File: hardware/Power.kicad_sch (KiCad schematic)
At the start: 26 parts, among them Q1 Q_NMOS, Q2 Q_NMOS, Q3 Q_NMOS, Q4 Q_NMOS, U5 BQ25798RQMR

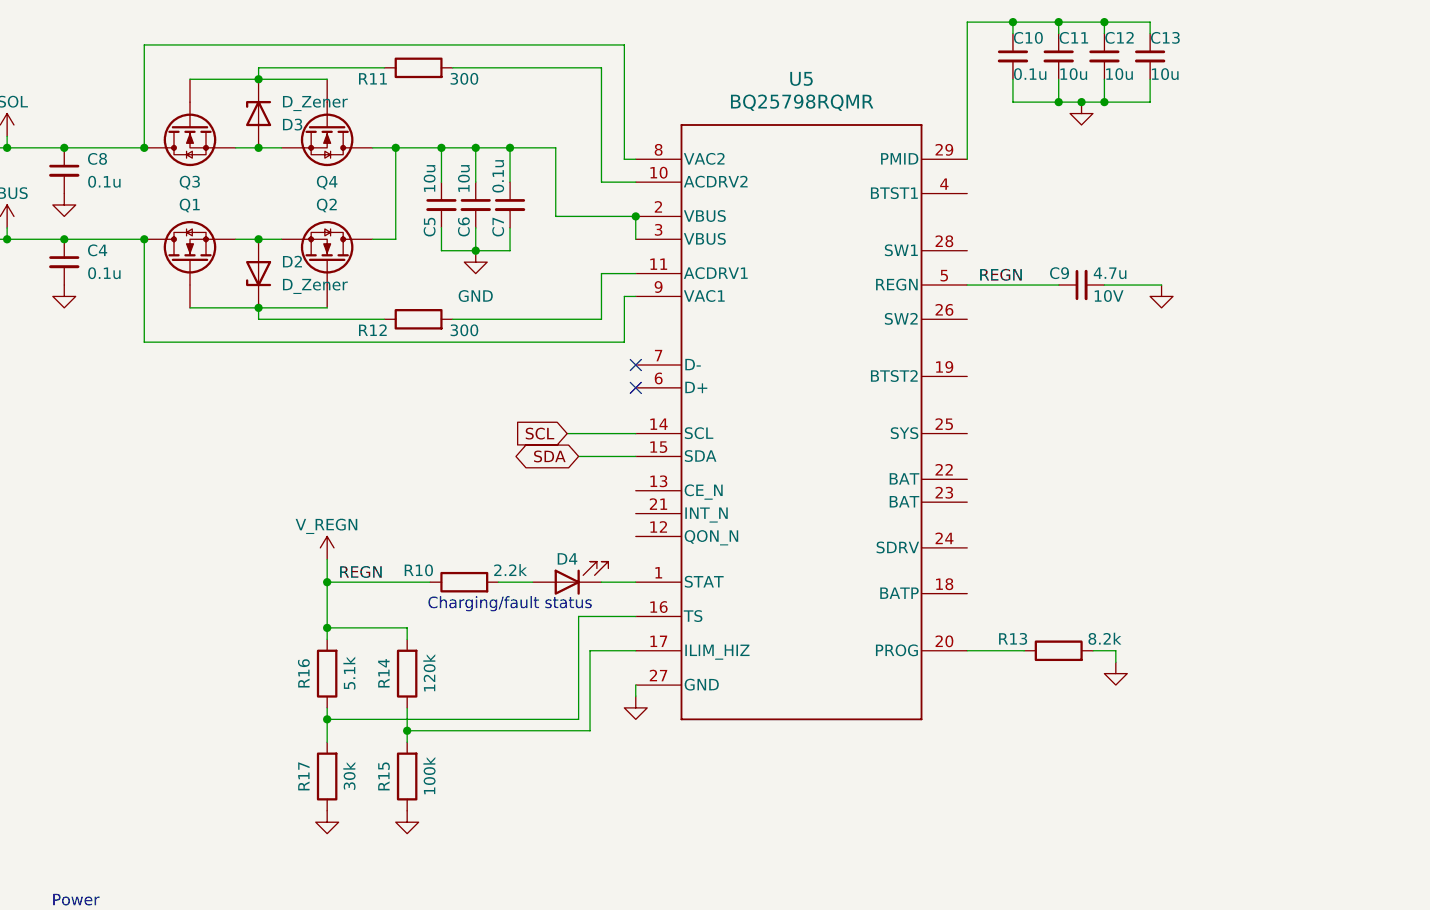
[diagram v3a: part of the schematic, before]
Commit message: Added BQ25798 integrated buck-boost inductor
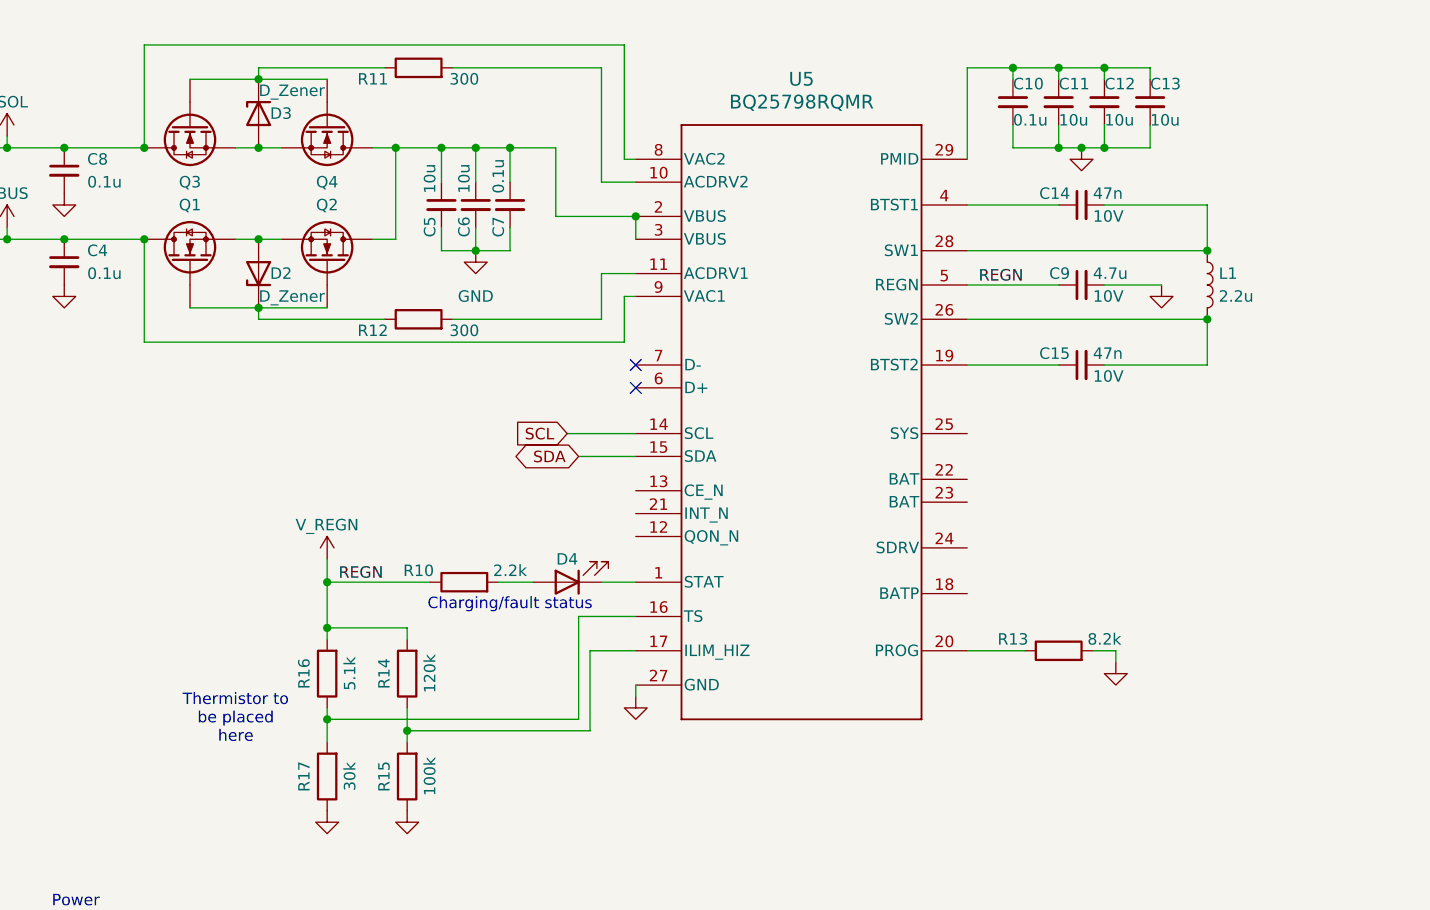
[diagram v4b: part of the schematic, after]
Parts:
- added C14, C15: 47n, Capacitor_SMD:C_0603_1608Metric, symbol Device:C_Small
- added L1: 2.2u, GoG_Library:MDA5030-2R2M, symbol Device:L
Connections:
- net at U5.19 (BTST2): now also C15.1
- net at U5.26 (SW2): now also C15.2, L1.2
- net at U5.28 (SW1): now also C14.2, L1.1
- net at U5.4 (BTST1): now also C14.1
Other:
- note added: "Thermistor to be placed here"
- moved on the sheet: C10, C11, C12, C13

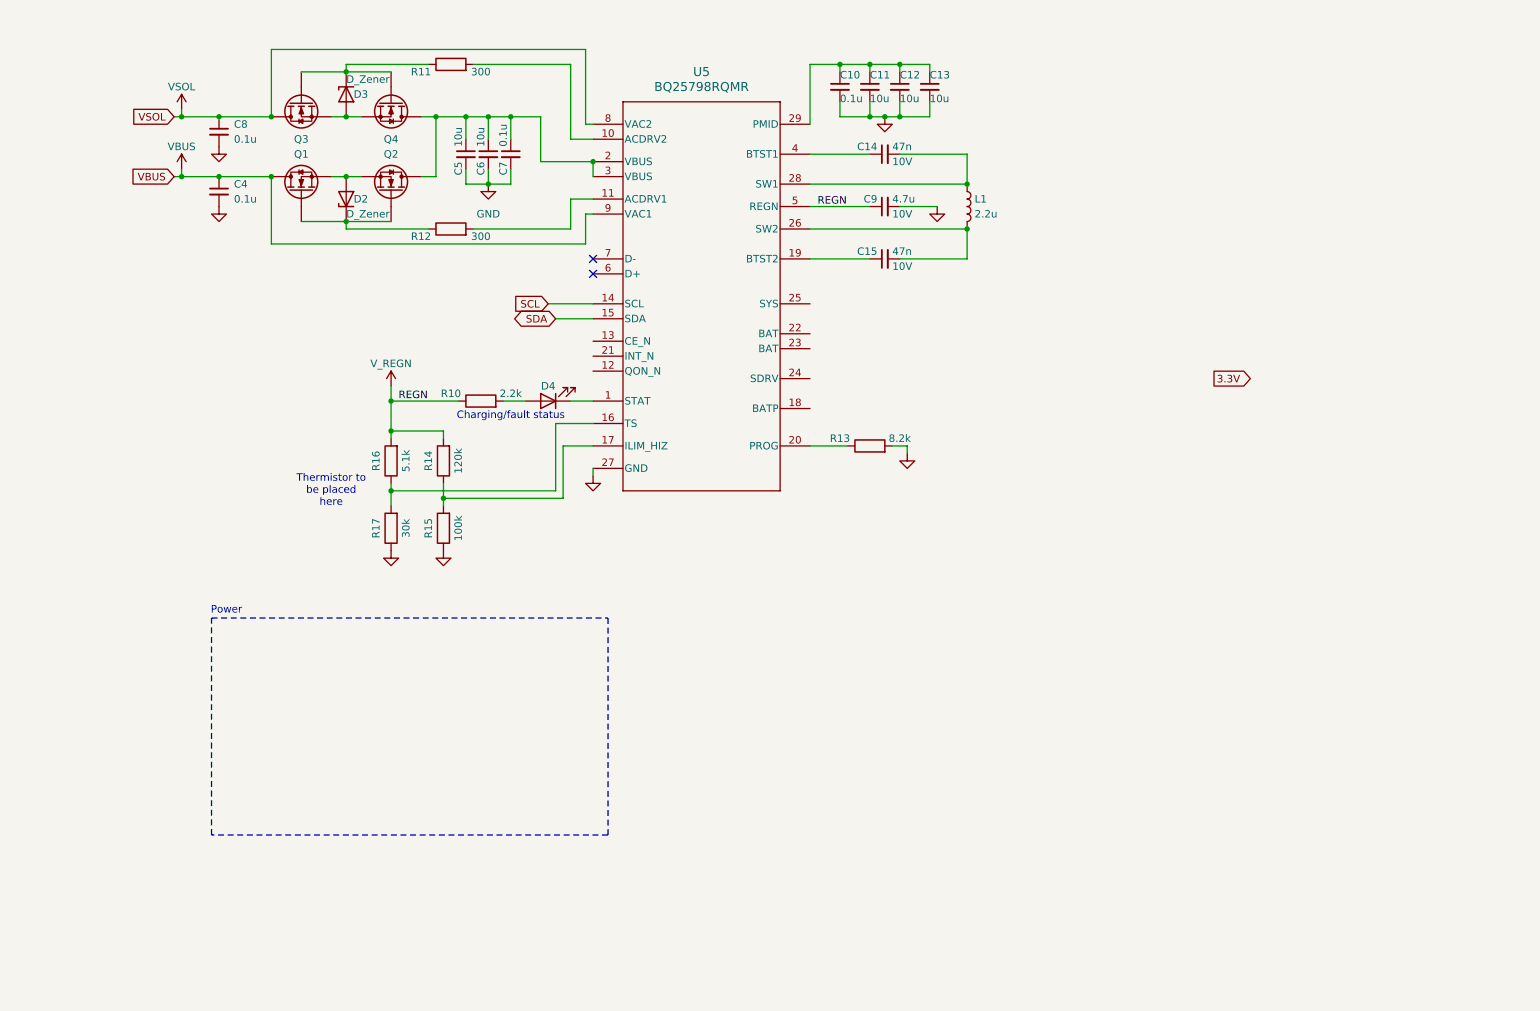
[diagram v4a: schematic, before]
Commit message: Add SYS output capacitors & cap. package sizes
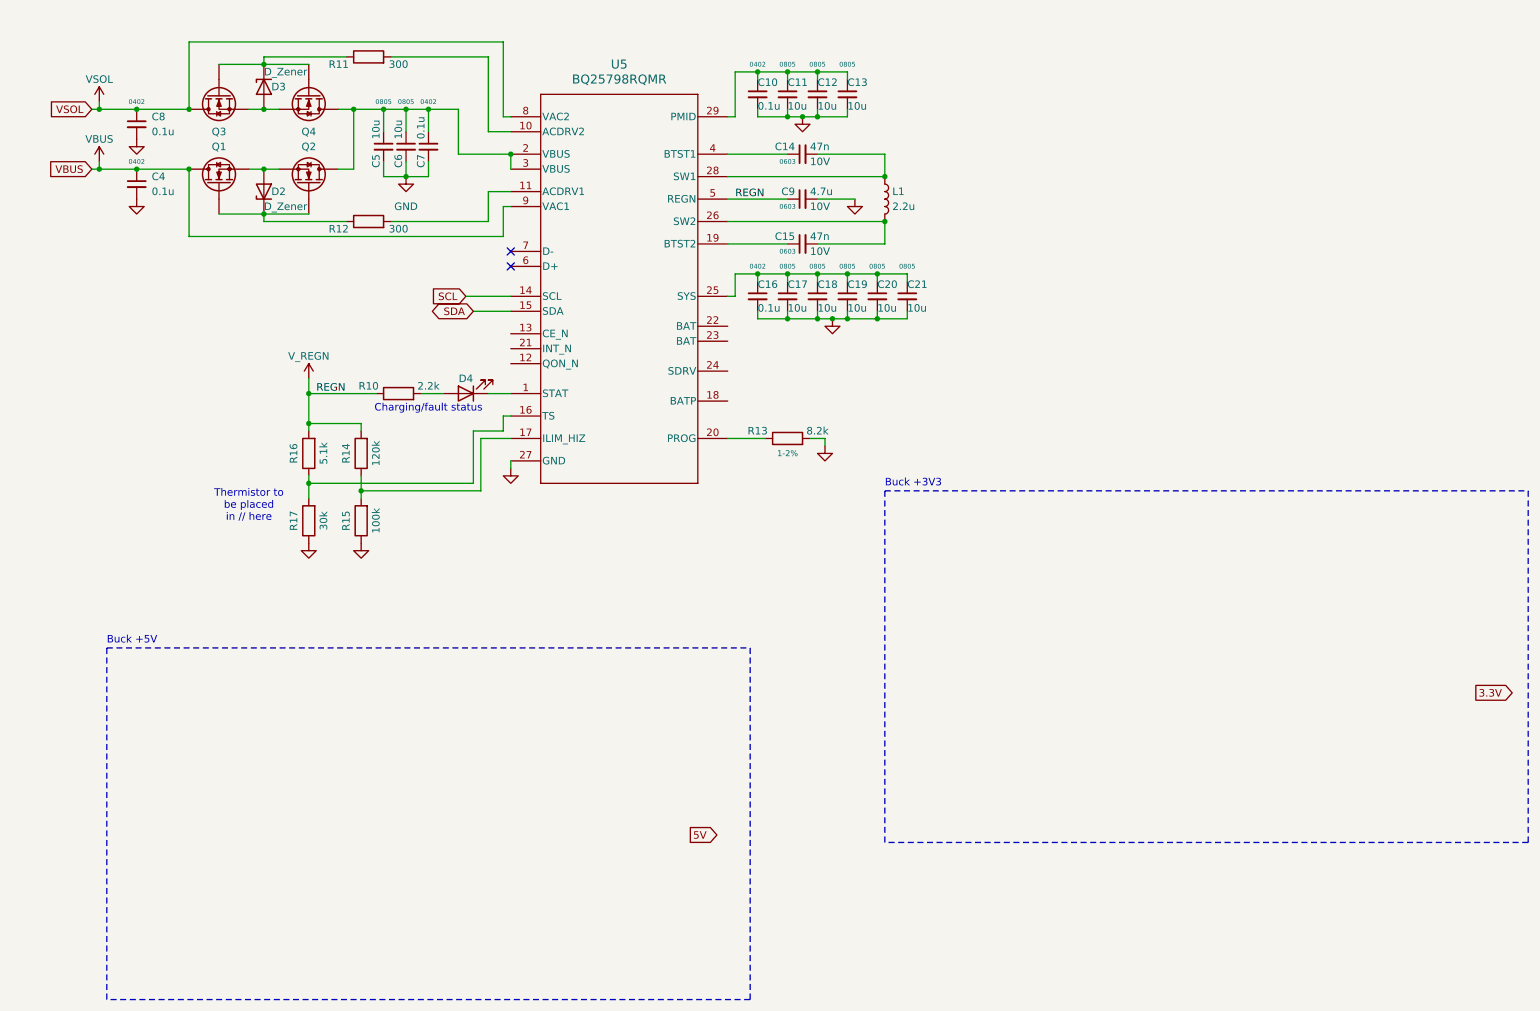
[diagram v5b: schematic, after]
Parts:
- added C16: 0.1u, Capacitor_SMD:C_0402_1005Metric, symbol Device:C_Small
- added C17, C18, C19, C20, C21: 10u, Capacitor_SMD:C_0805_2012Metric, symbol Device:C_Small
- C10, C4, C7, C8: Package (none) -> 0402
- C11, C12, C13, C5, C6: footprint Capacitor_SMD:C_0603_1608Metric -> Capacitor_SMD:C_0805_2012Metric; Package (none) -> 0805
- C14, C15, C9: Package (none) -> 0603
- R13: Tolerence (none) -> 1-2%
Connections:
- net GND: now also C16.2, C17.2, C18.2, C19.2, C20.2, C21.2
- net at U5.25 (SYS): now also C16.1, C17.1, C18.1, C19.1, C20.1, C21.1
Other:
- note added: "Buck +3V3"
- note added: "Buck +5V"
- note added: "Thermistor to be placed in // here"
- note removed: "Power"
- note removed: "Thermistor to be placed here"
- moved on the sheet: C10, C11, C12, C13, C14, C15, C4, C5, C6, C7, C8, C9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

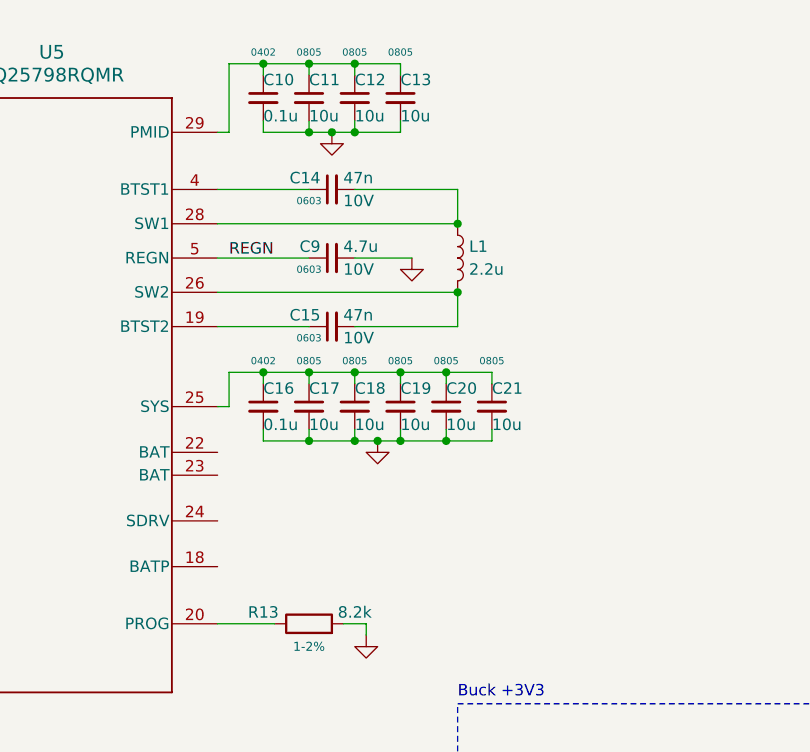
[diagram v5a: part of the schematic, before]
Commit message: Add 2S battery circuit
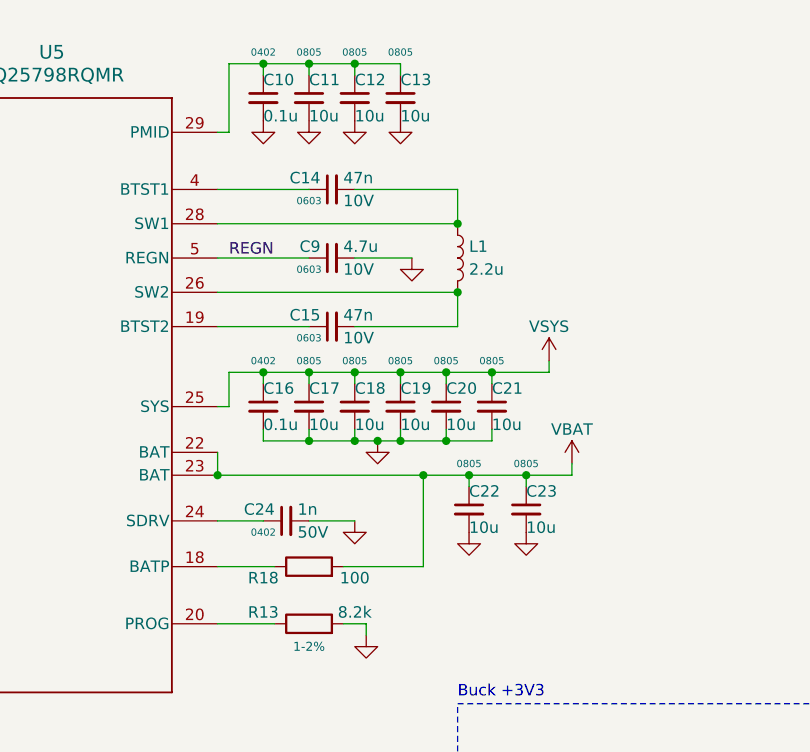
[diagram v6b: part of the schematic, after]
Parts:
- added C22, C23: 10u, Capacitor_SMD:C_0805_2012Metric, symbol Device:C_Small
- added C24: 1n, Capacitor_SMD:C_0402_1005Metric, symbol Device:C_Small
- added R18: 100, Resistor_SMD:R_0402_1005Metric, symbol Device:R
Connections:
- net GND: now also C22.2, C23.2, C24.2
- net VSYS: now reaches C16.1, C17.1, C18.1, C19.1, C20.1, C21.1, U5.25 (SYS)
- net at U5.18 (BATP): now also R18.1
- net VBAT: now reaches U5.22 (BAT)
- net VBAT: now also U5.23 (BAT), C22.1, C23.1, R18.2
- net at U5.24 (SDRV): now also C24.1
